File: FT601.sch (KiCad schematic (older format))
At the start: 12 parts, among them U1 FT601, X1 GSB443133HR

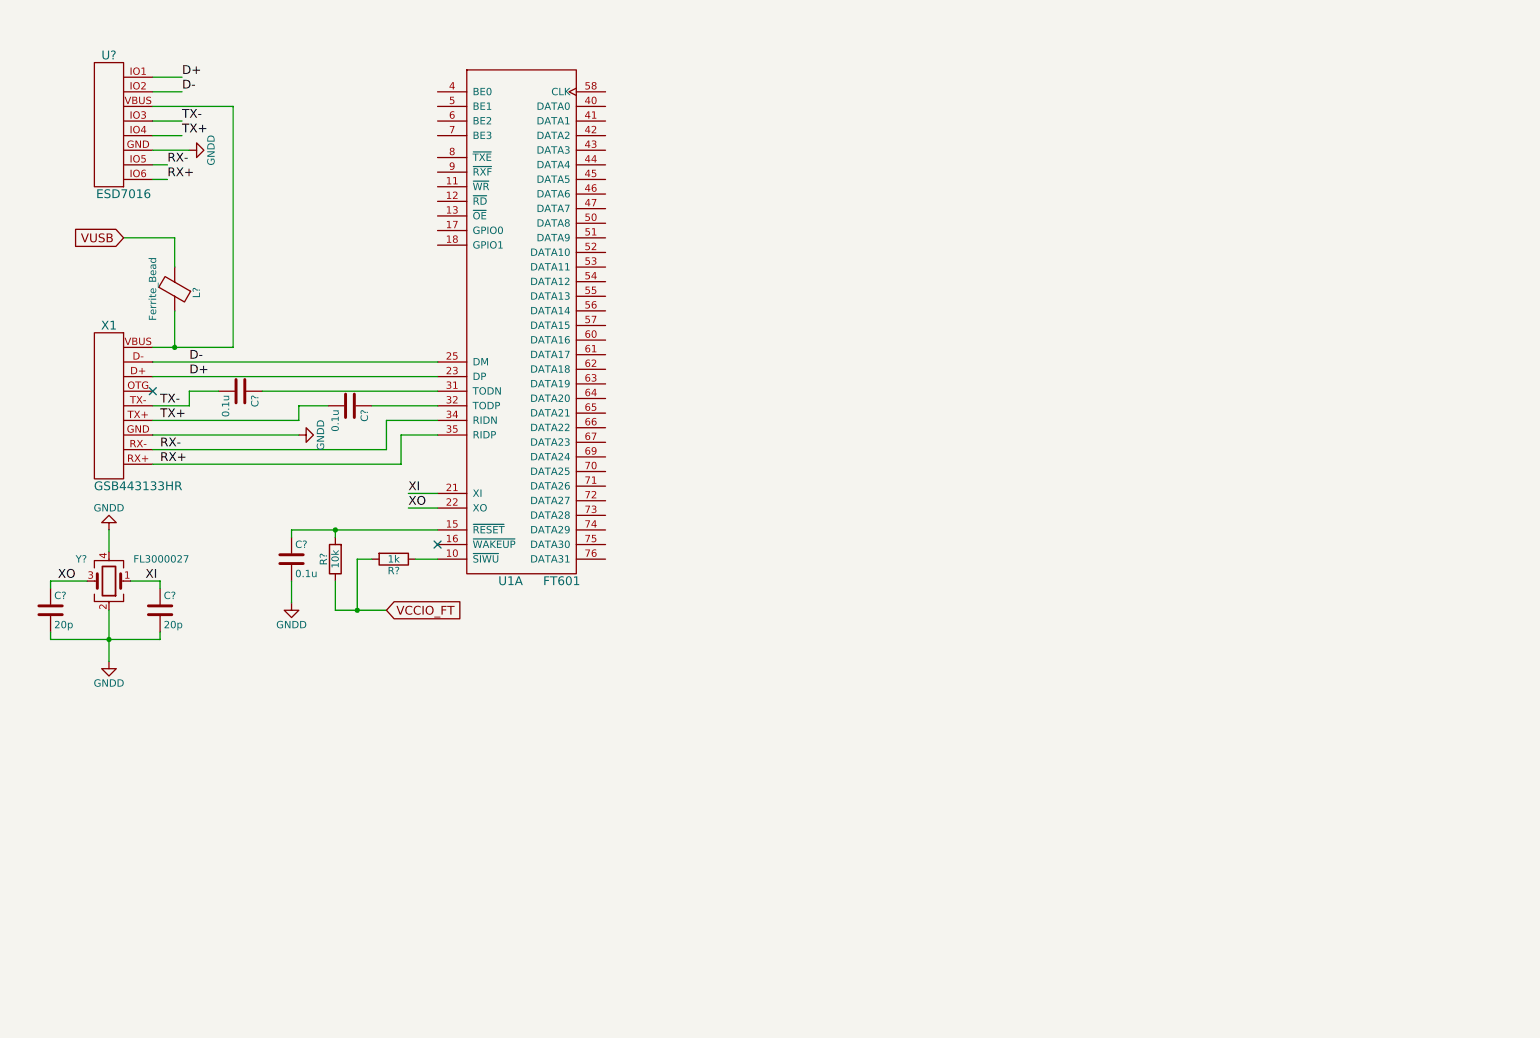
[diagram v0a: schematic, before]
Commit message: Cloack, LMS are added
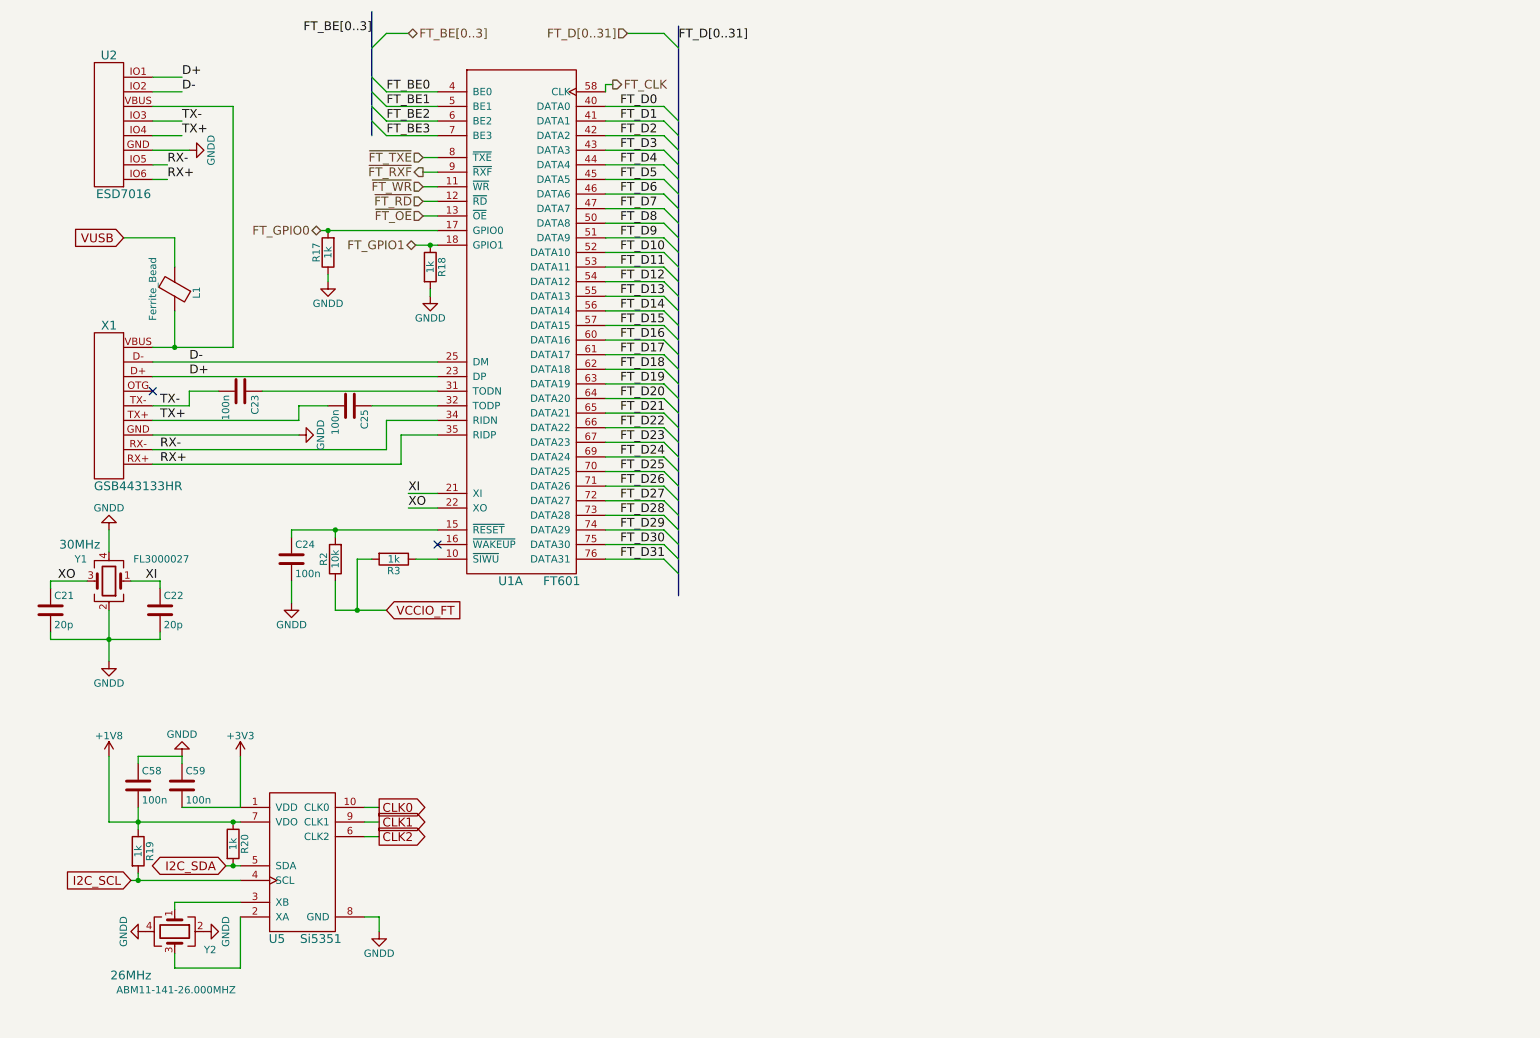
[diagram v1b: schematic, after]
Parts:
- added C58, C59: 100n, Capacitors_SMD:C_0603_HandSoldering, symbol C
- added R17, R18, R19, R20: 1k, Resistors_SMD:R_0603_HandSoldering, symbol R
- added U5: Si5351, Housings_SSOP:MSOP-10_3x3mm_Pitch0.5mm, symbol Si5351
- added Y2: ABM11-141-26.000MHZ, Crystals:Crystal_SMD_2016-4pin_2.0x1.6mm, symbol Crystal_GND24
- C21, C22: renamed from C?; footprint (none) -> Capacitors_SMD:C_0603_HandSoldering
- C23, C24, C25: renamed from C?; value 0.1u -> 100n; footprint (none) -> Capacitors_SMD:C_0603_HandSoldering
- L1: renamed from L?; footprint (none) -> Inductors_SMD:L_0603_HandSoldering
- R2, R3: renamed from R?; footprint (none) -> Resistors_SMD:R_0603_HandSoldering
- Y1: renamed from Y?; footprint Crystals:Crystal_SMD_3225-4pin_3.2x2.5mm_HandSoldering -> Crystals:Crystal_SMD_3225-4pin_3.2x2.5mm; Frequency (none) -> 30MHz
- gave numbers to parts that had none: 1
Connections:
- net GNDD: now also C58.1, C59.1, R17.1, R18.2, U5.8 (GND), Y2.2, Y2.4
- net ~FT_WR: now reaches U1.11 (~WR)
- net ~FT_RD: now reaches U1.12 (~RD)
- net ~FT_OE: now reaches U1.13 (~OE)
- net FT_GPIO0: now reaches U1.17 (GPIO0)
- net FT_GPIO0: now also R17.2
- net FT_GPIO1: now reaches U1.18 (GPIO1)
- net FT_GPIO1: now also R18.1
- net FT_BE0: now reaches U1.4 (BE0)
- net FT_D0: now reaches U1.40 (DATA0)
- net FT_D1: now reaches U1.41 (DATA1)
- net FT_D2: now reaches U1.42 (DATA2)
- net FT_D3: now reaches U1.43 (DATA3)
- net FT_D4: now reaches U1.44 (DATA4)
- net FT_D5: now reaches U1.45 (DATA5)
- net FT_D6: now reaches U1.46 (DATA6)
- net FT_D7: now reaches U1.47 (DATA7)
- net FT_BE1: now reaches U1.5 (BE1)
- net FT_D8: now reaches U1.50 (DATA8)
- net FT_D9: now reaches U1.51 (DATA9)
- net FT_D10: now reaches U1.52 (DATA10)
- net FT_D11: now reaches U1.53 (DATA11)
- net FT_D12: now reaches U1.54 (DATA12)
- net FT_D13: now reaches U1.55 (DATA13)
- net FT_D14: now reaches U1.56 (DATA14)
- net FT_D15: now reaches U1.57 (DATA15)
- net FT_CLK: now reaches U1.58 (CLK)
- net FT_BE2: now reaches U1.6 (BE2)
- net FT_D16: now reaches U1.60 (DATA16)
- net FT_D17: now reaches U1.61 (DATA17)
- net FT_D18: now reaches U1.62 (DATA18)
- net FT_D19: now reaches U1.63 (DATA19)
- net FT_D20: now reaches U1.64 (DATA20)
- net FT_D21: now reaches U1.65 (DATA21)
- net FT_D22: now reaches U1.66 (DATA22)
- net FT_D23: now reaches U1.67 (DATA23)
- net FT_D24: now reaches U1.69 (DATA24)
- net FT_BE3: now reaches U1.7 (BE3)
- net FT_D25: now reaches U1.70 (DATA25)
- net FT_D26: now reaches U1.71 (DATA26)
- net FT_D27: now reaches U1.72 (DATA27)
- net FT_D28: now reaches U1.73 (DATA28)
- net FT_D29: now reaches U1.74 (DATA29)
- net FT_D30: now reaches U1.75 (DATA30)
- net FT_D31: now reaches U1.76 (DATA31)
- net ~FT_TXE: now reaches U1.8 (~TXE)
- net ~FT_RXF: now reaches U1.9 (~RXF)
- new net: U5.2 (XA), Y2.3
- new net: U5.3 (XB), Y2.1
- new net +1V8: C58.2, R19.1, R20.1, U5.7 (VDO)
- new net +3V3: C59.2, U5.1 (VDD)
- new net CLK0: U5.10 (CLK0)
- new net CLK1: U5.9 (CLK1)
- new net CLK2: U5.6 (CLK2)
- new net I2C_SCL: R19.2, U5.4 (SCL)
- new net I2C_SDA: R20.2, U5.5 (SDA)

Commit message: Schematic is done except RF.
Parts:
- C21, C22, C23, C24, C25, C58, C59: footprint Capacitors_SMD:C_0603_HandSoldering -> Capacitors_SMD:C_0402
- R17, R18, R19, R2, R20, R3: footprint Resistors_SMD:R_0603_HandSoldering -> Resistors_SMD:R_0402
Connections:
- net +1V8: now also C59.1; no longer C58.2
- net +3V3: now also C58.1; no longer C59.2
- net GNDD: now also C58.2, C59.2; no longer C58.1, C59.1
- net VUSB: now also L1.1, U2.VBUS, X1.VBUS; no longer L1.2
- new net +5V: L1.2
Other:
- moved on the sheet: C58, C59, R19, R20, U5, Y2

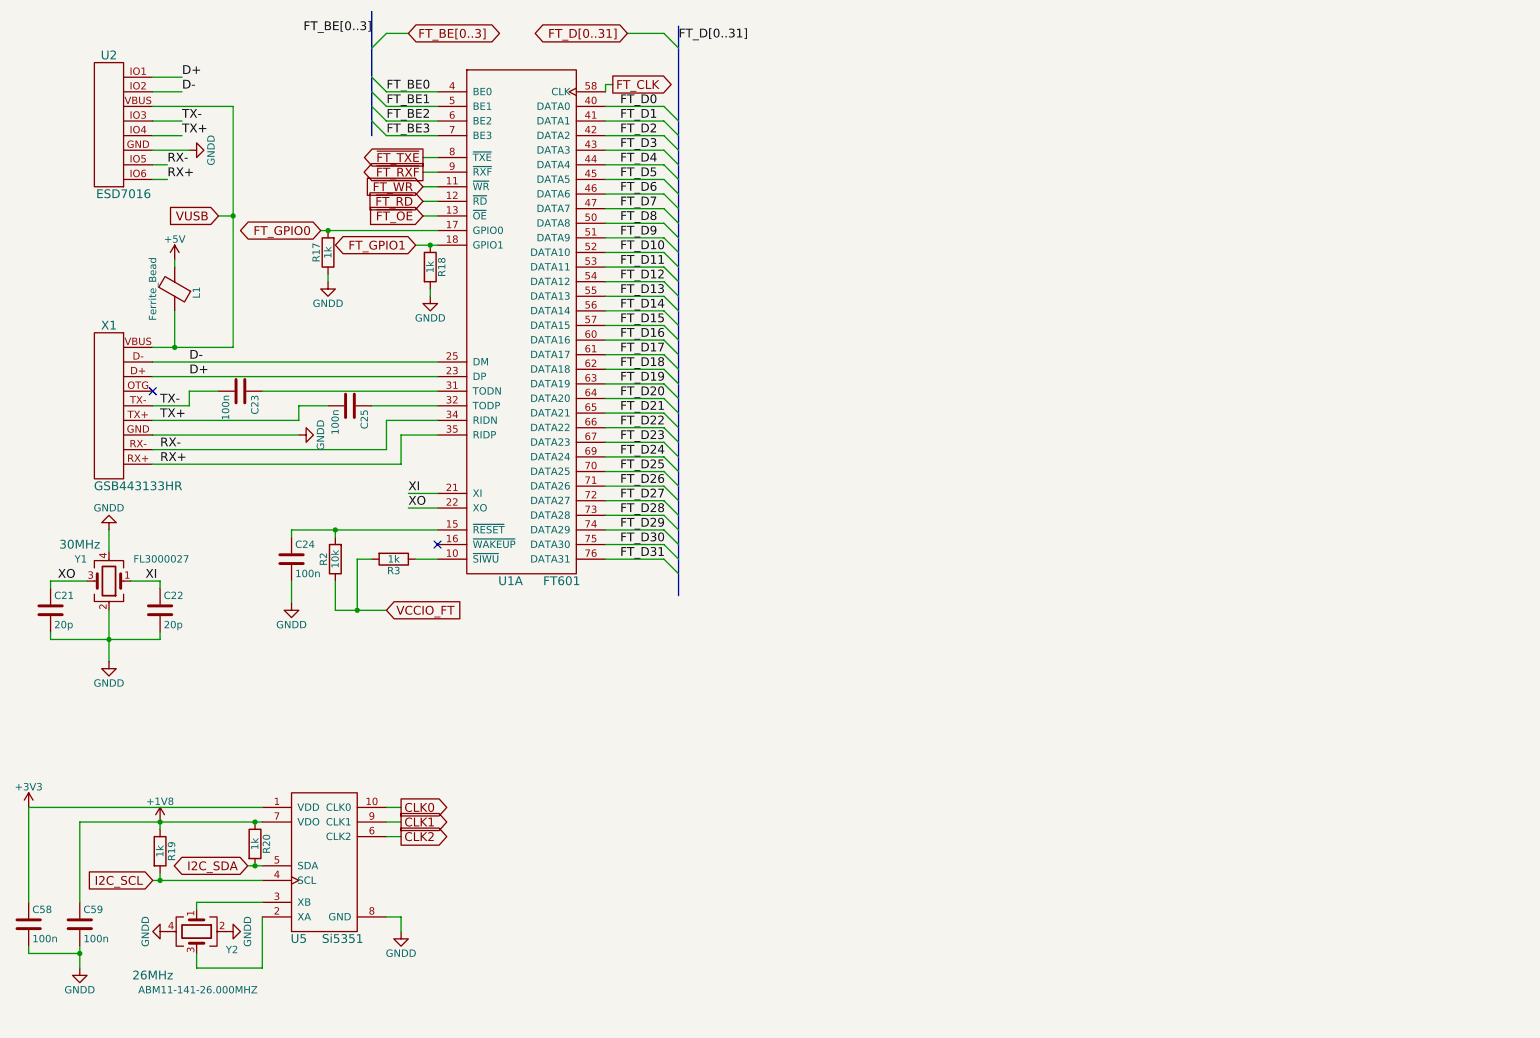
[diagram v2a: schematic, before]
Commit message: Placed most components for FTDI. Begin tracing FT601
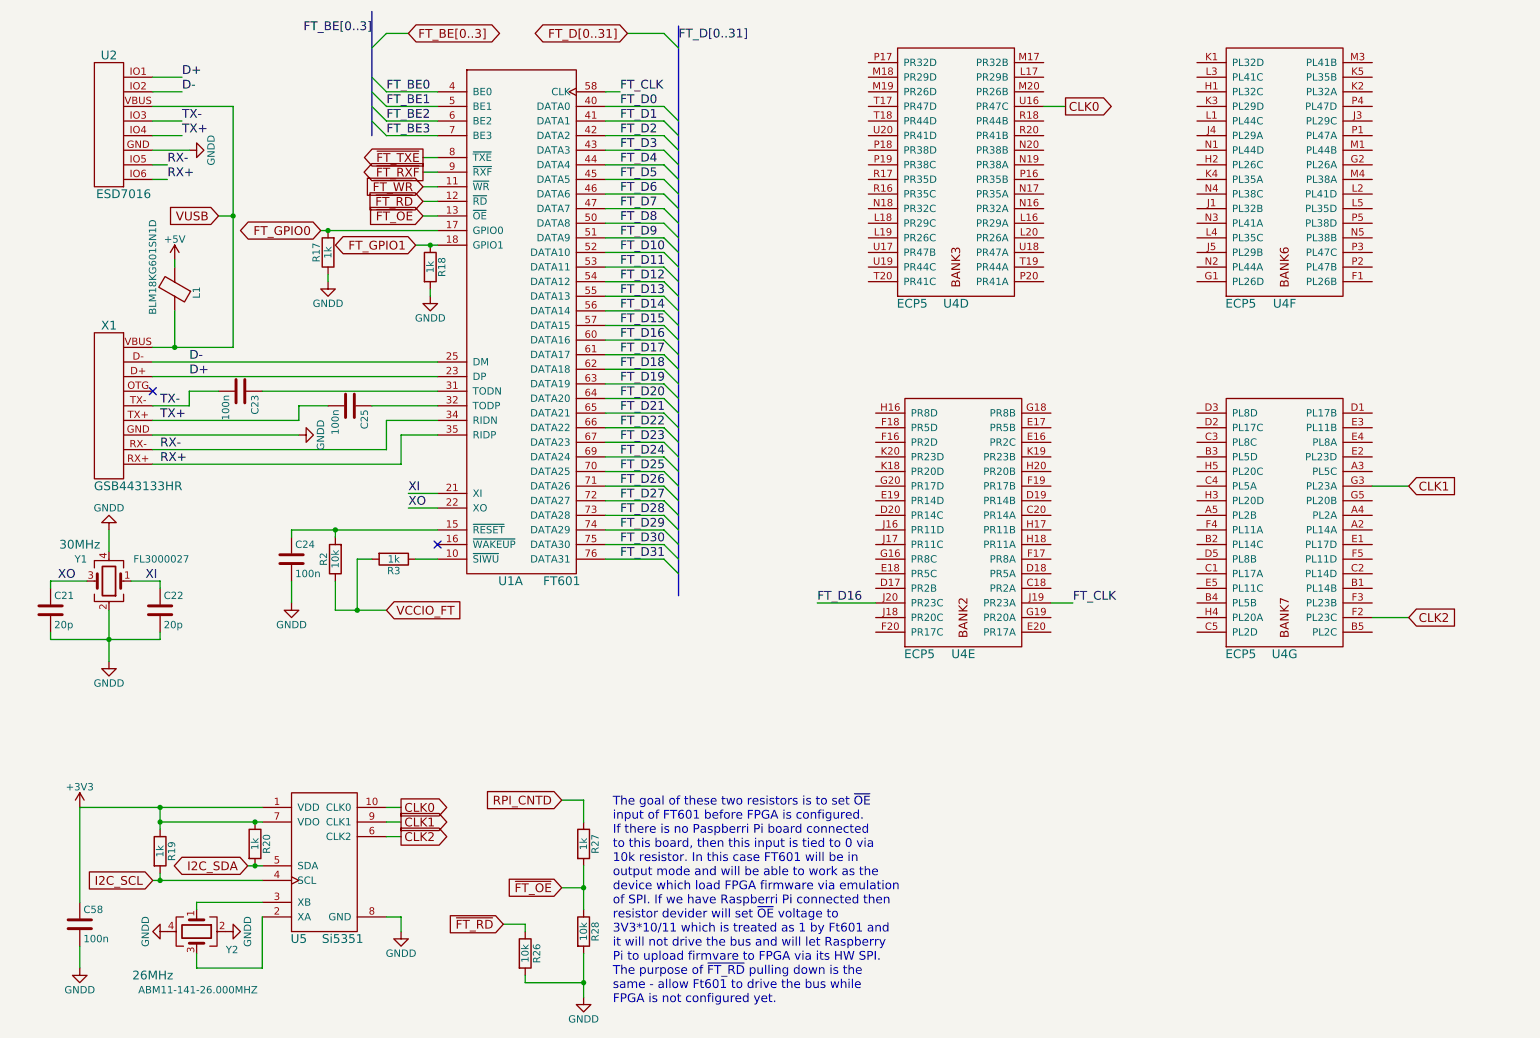
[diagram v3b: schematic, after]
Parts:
- removed C59: 100n, Capacitors_SMD:C_0402, symbol C
- added R26, R28: 10k, Resistors_SMD:R_0603, symbol R
- added R27: 1k, Resistors_SMD:R_0603, symbol R
- added U4: ECP5, sdr-foots:ECP5_381, symbol ECP5
- C21, C22, C23, C24, C25, C58: footprint Capacitors_SMD:C_0402 -> Capacitors_SMD:C_0603
- L1: value Ferrite_Bead -> BLM18KG601SN1D; footprint Inductors_SMD:L_0603_HandSoldering -> Capacitors_SMD:C_0805
- R17, R18, R19, R2, R20, R3: footprint Resistors_SMD:R_0402 -> Resistors_SMD:R_0603
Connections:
- net +1V8 is gone; now on net +3V3: R19.1, R20.1, U5.7 (VDO)
- net CLK0: now also U4.U16 (PR47C)
- net CLK1: now also U4.G3 (PL23A)
- net CLK2: now also U4.F2 (PL23C)
- net FT_CLK: now also U4.J19 (PR23A)
- net FT_D16: now also U4.J20 (PR23C)
- net GNDD: now also R26.2, R28.2
- net ~FT_OE: now also R27.2, R28.1
- net ~FT_RD: now also R26.1
- new net RPI_CNTD: R27.1
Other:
- note added: "The goal of these two resistors is to set ~OE~\ninput of FT601 before FPGA is configured.\nIf there is no Paspberri Pi board connected\nto this board, then this input is tied to 0 via\n10k resistor. In this case FT601 will be in\noutput mode and will be able to work as the\ndevice which load FPGA firmware via emulation\nof SPI. If we have Raspberri Pi connected then \nresistor devider will set ~O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"
- moved on the sheet: C58

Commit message: Right before Sitch power retracing
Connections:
- net FT_BE0: now also U4.U19 (PR44C)
- net FT_BE1: now also U4.T18 (PR44D)
- net FT_BE2: now also U4.U18 (PR47A)
- net FT_BE3: now also U4.U17 (PR47B)
- net FT_D10: now also U4.E20 (PR17A)
- net FT_D11: now also U4.F19 (PR17B)
- net FT_D12: now also U4.F20 (PR17C)
- net FT_D13: now also U4.G20 (PR17D)
- net FT_D14: now also U4.H20 (PR20B)
- net FT_D15: now also U4.H18 (PR11A)
- net FT_D17: now also U4.J18 (PR20C)
- net FT_D18: now also U4.K20 (PR23D)
- net FT_D19: now also U4.K19 (PR23B)
- net FT_D20: now also U4.L20 (PR26A)
- net FT_D21: now also U4.L19 (PR26C)
- net FT_D22: now also U4.M20 (PR26B)
- net FT_D23: now also U4.M19 (PR26D)
- net FT_D24: now also U4.N20 (PR38B)
- net FT_D25: now also U4.N19 (PR38A)
- net FT_D26: now also U4.P20 (PR41A)
- net FT_D27: now also U4.P19 (PR38C)
- net FT_D28: now also U4.R20 (PR41B)
- net FT_D29: now also U4.R18 (PR44B)
- net FT_D30: now also U4.T20 (PR41C)
- net FT_D31: now also U4.T19 (PR44A)
- net FT_D6: now also U4.C20 (PR14A)
- net FT_D7: now also U4.D19 (PR14B)
- net FT_D8: now also U4.D20 (PR14C)
- net FT_D9: now also U4.E19 (PR14D)
- net ~FT_OE: now also U4.P18 (PR38D)
- net ~FT_RD: now also U4.N18 (PR32C)
- net ~FT_WR: now also U4.U20 (PR41D)
- no-connect marks 2 -> 8
